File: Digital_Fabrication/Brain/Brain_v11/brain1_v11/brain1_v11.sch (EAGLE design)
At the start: 90 parts, among them J6 ELECTRO_MECH_PAD, J7 ELECTRO_MECH_PAD, J8 ELECTRO_MECH_PAD, J9 ELECTRO_MECH_PAD

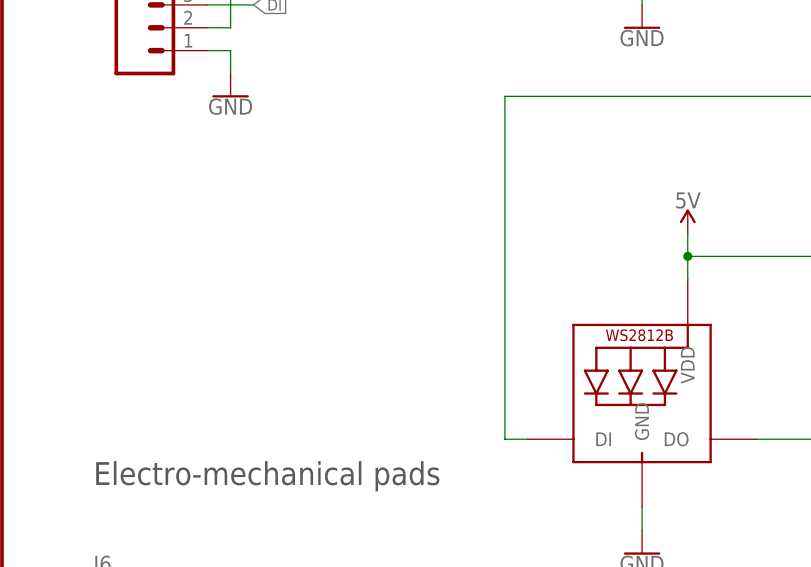
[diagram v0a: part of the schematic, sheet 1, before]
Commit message: Add silkscreen
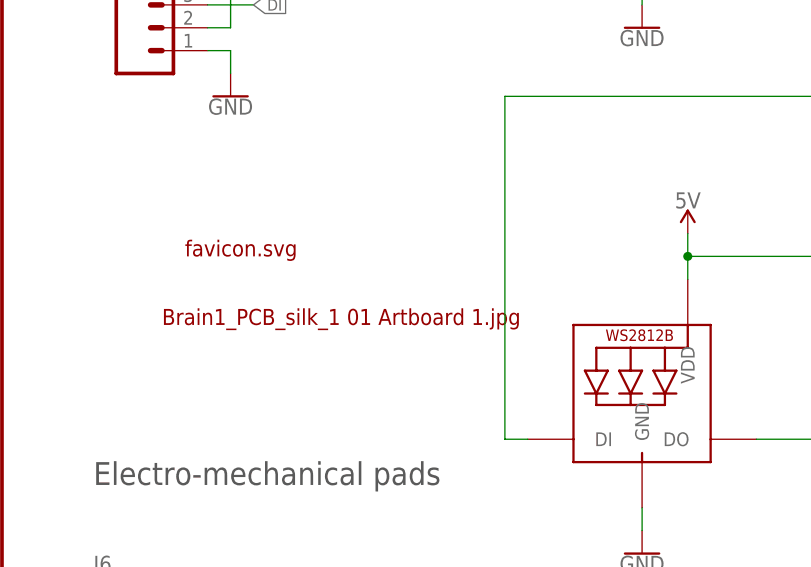
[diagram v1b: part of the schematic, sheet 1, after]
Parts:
- added U$1: FAVICON#SVG, favicon#svg:FAVICON#SVG
- added U$2: BRAIN1_PCB_SILK_1_01_ARTBOARD_1#JPG, Brain1_PCB_silk_1_01_Artboard_1#jpg:BRAIN1_PCB_SILK_1_01_ARTBOARD_1#JPG
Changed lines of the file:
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@@
 <?xml version="1.0" encoding="utf-8"?>
 <!DOCTYPE eagle SYSTEM "eagle.dtd">
-<eagle version="9.5.2">
+<eagle version="9.6.2">
 <drawing>
 <settings>
@@
 <part name="J8" library="brain" deviceset="ELECTRO_MECH_PAD" device=""/>
 <part name="J9" library="brain" deviceset="ELECTRO_MECH_PAD" device=""/>
+<part name="U$1" library="favicon#svg" deviceset="FAVICON#SVG" device=""/>
+<part name="U$2" library="Brain1_PCB_silk_1_01_Artboard_1#jpg" deviceset="BRAIN1_PCB_SILK_1_01_ARTBOARD_1#JPG" device=""/>
 </parts>
 <sheets>
@@
 <attribute name="NAME" x="10.16" y="76.708" size="1.778" layer="95" font="vector"/>
 </instance>
+<instance part="U$1" gate="G$1" x="22.86" y="154.94" smashed="yes"/>
+<instance part="U$2" gate="G$1" x="20.32" y="147.32" smashed="yes"/>
 </instances>
 <busses>

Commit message: brain boards v11
Added custom silkscreen
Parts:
- added U$10: 5V1, brain:5V1
- added U$11: GND0, brain:GND0
- added U$12: DI0, brain:DI0
- added U$13: DO3, brain:DO3
- added U$14: IN0, buzzard_labels (8):IN0
- added U$15: OUT1, buzzard_labels (8):OUT1
- added U$3: MAKIN_STUFF2, buzzard_labels (5):MAKIN_STUFF2
- added U$4: A_NERVOUS0, buzzard_labels (5):A_NERVOUS0
- added U$5: SYSTEM1, buzzard_labels (5):SYSTEM1
- added U$6: 5V1, buzzard_labels (6):5V1
- added U$7: GND0, buzzard_labels (6):GND0
- added U$8: DO3, buzzard_labels (6):DO3
- added U$9: DI0, buzzard_labels (7):DI0
- U$1: value FAVICON#SVG -> BRAIN1_PCB_BOT_SILK; device favicon#svg:FAVICON#SVG -> brain:BRAIN1_PCB_BOT_SILK
- U$2: value BRAIN1_PCB_SILK_1_01_ARTBOARD_1#JPG -> BRAIN1_PCB_TOP_SILK; device Brain1_PCB_silk_1_01_Artboard_1#jpg:BRAIN1_PCB_SILK_1_01_ARTBOARD_1#JPG -> brain:BRAIN1_PCB_TOP_SILK
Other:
- note added: "Aesthetics"
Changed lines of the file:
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@@
 <part name="J8" library="brain" deviceset="ELECTRO_MECH_PAD" device=""/>
 <part name="J9" library="brain" deviceset="ELECTRO_MECH_PAD" device=""/>
-<part name="U$1" library="favicon#svg" deviceset="FAVICON#SVG" device=""/>
-<part name="U$2" library="Brain1_PCB_silk_1_01_Artboard_1#jpg" deviceset="BRAIN1_PCB_SILK_1_01_ARTBOARD_1#JPG" device=""/>
+<part name="U$2" library="brain" deviceset="BRAIN1_PCB_TOP_SILK" device=""/>
+<part name="U$1" library="brain" deviceset="BRAIN1_PCB_BOT_SILK" device=""/>
+<part name="U$3" library="buzzard_labels (5)" deviceset="MAKIN_STUFF2" device=""/>
+<part name="U$4" library="buzzard_labels (5)" deviceset="A_NERVOUS0" device=""/>
+<part name="U$5" library="buzzard_labels (5)" deviceset="SYSTEM1" device=""/>
+<part name="U$6" library="buzzard_labels (6)" deviceset="5V1" device=""/>
+<part name="U$7" library="buzzard_labels (6)" deviceset="GND0" device=""/>
+<part name="U$8" library="buzzard_labels (6)" deviceset="DO3" device=""/>
+<part name="U$9" library="buzzard_labels (7)" deviceset="DI0" device=""/>
+<part name="U$10" library="brain" deviceset="5V1" device=""/>
+<part name="U$11" library="brain" deviceset="GND0" device=""/>
+<part name="U$12" library="brain" deviceset="DI0" device=""/>
+<part name="U$13" library="brain" deviceset="DO3" device=""/>
+<part name="U$14" library="buzzard_labels (8)" deviceset="IN0" device=""/>
+<part name="U$15" library="buzzard_labels (8)" deviceset="OUT1" device=""/>
 </parts>
 <sheets>
@@
 <text x="10.16" y="198.12" size="2.54" layer="97" font="vector">Headers</text>
 <text x="10.16" y="129.54" size="2.54" layer="97" font="vector">Electro-mechanical pads</text>
+<text x="5.08" y="25.4" size="2.54" layer="97" font="vector">Aesthetics</text>
 </plain>
 <instances>
@@
 <attribute name="NAME" x="10.16" y="76.708" size="1.778" layer="95" font="vector"/>
 </instance>
-<instance part="U$1" gate="G$1" x="22.86" y="154.94" smashed="yes"/>
-<instance part="U$2" gate="G$1" x="20.32" y="147.32" smashed="yes"/>
+<instance part="U$2" gate="G$1" x="5.08" y="10.16" smashed="yes"/>
+<instance part="U$1" gate="G$1" x="5.08" y="5.08" smashed="yes"/>
+<instance part="U$3" gate="G$1" x="35.56" y="5.08" smashed="yes"/>
+<instance part="U$4" gate="G$1" x="35.56" y="15.24" smashed="yes"/>
+<instance part="U$5" gate="G$1" x="35.56" y="10.16" smashed="yes"/>
+<instance part="U$6" gate="G$1" x="55.88" y="20.32" smashed="yes"/>
+<instance part="U$7" gate="G$1" x="55.88" y="15.24" smashed="yes"/>
+<instance part="U$8" gate="G$1" x="55.88" y="10.16" smashed="yes"/>
+<instance part="U$9" gate="G$1" x="55.88" y="5.08" smashed="yes"/>
+<instance part="U$10" gate="G$1" x="66.04" y="20.32" smashed="yes"/>
+<instance part="U$11" gate="G$1" x="66.04" y="15.24" smashed="yes"/>
+<instance part="U$12" gate="G$1" x="66.04" y="5.08" smashed="yes"/>
+<instance part="U$13" gate="G$1" x="66.04" y="10.16" smashed="yes"/>
+<instance part="U$14" gate="G$1" x="78.74" y="10.16" smashed="yes"/>
+<instance part="U$15" gate="G$1" x="78.74" y="5.08" smashed="yes"/>
 </instances>
 <busses>
